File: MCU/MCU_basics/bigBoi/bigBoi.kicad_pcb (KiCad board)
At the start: 2 copper layers, 62 x 62 mm, 86 parts, among them IC1 BMP390, J3 DM3AT-SF-PEJM5_40_, J4 Conn_01x05, J5 Conn_01x04, J6 Conn_01x06, J7 USB_B_Micro, SW1 Boot Switch, U1 STM32F469NIHx, U2 LT1963AxST-3.3, U3 SX1276, U5 MIA-M10Q, U6 BNO086, Y1 8MHz, Y3 32kHz

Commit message: update nebula FP
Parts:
- removed C1, C10, C12, C15, C16, C19, C2, C20, C22, C23, C24, C25, C26, C3, C30, C35, C37, C39, C4, C48, C49, C5, C50, C51, C52, C54, C6, C7, C8, C9: 100nF, Capacitor_SMD:C_0402_1005Metric
- removed C11: 10nF, Capacitor_SMD:C_0402_1005Metric
- removed C13, C29, C31, C32, C38: 1uF, Capacitor_SMD:C_0402_1005Metric
- removed C14, C18: 0402, Capacitor_SMD:C_0402_1005Metric
- removed C17, C21: 2.2uF, Capacitor_SMD:C_0603_1608Metric
- removed C27, C59: 10uF, Capacitor_SMD:C_0805_2012Metric
- removed C28, C47: 15pF, Capacitor_SMD:C_0402_1005Metric
- removed C33, C34: 22uF, Capacitor_SMD:C_0805_2012Metric
- removed C36: 10uF, Capacitor_SMD:C_0603_1608Metric
- removed C40, C41, C43: 0.1uF, Capacitor_SMD:C_0402_1005Metric
- removed C42: 22pF, Capacitor_SMD:C_0402_1005Metric
- removed C44: 22PF, Capacitor_SMD:C_0402_1005Metric
- removed C45, C46: 100nf, Capacitor_SMD:C_0402_1005Metric
- removed C53, C58: 47pF, Capacitor_SMD:C_0402_1005Metric
- removed C55: 1.5pF, Capacitor_SMD:C_0402_1005Metric
- removed C56: 4.7pF, Capacitor_SMD:C_0402_1005Metric
- removed C57: 1nF, Capacitor_SMD:C_0402_1005Metric
- removed D1: 1N914, Diode_THT:D_DO-35_SOD27_P7.62mm_Horizontal
- removed D2: GREEN, LED_SMD:LED_0603_1608Metric
- removed FB1: 120R, Inductor_SMD:L_0603_1608Metric
- removed IC1: BMP390, Nebula-footprints:BMP390
- removed J3: DM3AT-SF-PEJM5_40_, Nebula-footprints:DM3ATSFPEJM540
- removed J4: Conn_01x05, Connector_PinHeader_2.54mm:PinHeader_1x05_P2.54mm_Vertical
- removed J5: Conn_01x04, Connector_PinHeader_2.54mm:PinHeader_1x04_P2.54mm_Vertical
- removed J6: Conn_01x06, Connector_PinHeader_2.54mm:PinHeader_1x06_P2.54mm_Vertical
- removed J7: USB_B_Micro, Connector_USB:USB_Micro-B_Molex_47346-0001
- removed R1, R2, R3, R4: 10k, Resistor_SMD:R_0402_1005Metric
- removed R5, R6: 2.2k, Resistor_SMD:R_0402_1005Metric
- removed R7: 1k5, Resistor_SMD:R_0402_1005Metric
- removed the REF** at (152.3, 118.0)
- removed the REF** at (105.5, 118.0)
- removed SW1: Boot Switch, Button_Switch_SMD:SW_SPDT_PCM12
- removed U1: STM32F469NIHx, Package_BGA:TFBGA-216_13x13mm_Layout15x15_P0.8mm
- removed U2: LT1963AxST-3.3, Package_TO_SOT_SMD:SOT-223-3_TabPin2
- removed U3: SX1276, Package_DFN_QFN:QFN-28-1EP_6x6mm_P0.65mm_EP4.8x4.8mm
- removed U5: MIA-M10Q, Package_LGA:ublox_LGA-53_4.5x4.5mm_Layout9x9_P0.5mm
- removed U6: BNO086, Nebula-footprints:BNO086
- removed Y1: 8MHz, Crystal:Crystal_SMD_3225-4Pin_3.2x2.5mm_HandSoldering
- removed Y3: 32kHz, Crystal:Crystal_SMD_3215-2Pin_3.2x1.5mm

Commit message: Bat
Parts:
- removed the REF** at (128.9, 77.5)
- added REF**: MountingHole_3.2mm_M3, MountingHole:MountingHole_3.2mm_M3, F.Cu at (140.0, 100.0)
- added REF**: MountingHole_3.2mm_M3, MountingHole:MountingHole_3.2mm_M3, F.Cu at (108.0, 132.0)
- added REF**: MountingHole_3.2mm_M3, MountingHole:MountingHole_3.2mm_M3, F.Cu at (108.0, 68.0)
- added REF**: MountingHole_3.2mm_M3, MountingHole:MountingHole_3.2mm_M3, F.Cu at (76.0, 100.0)
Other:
- board size 62 x 62 mm -> 70 x 70 mm

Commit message: small changes
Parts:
- added BT1: Battery, Connector_JST:JST_PH_S2B-PH-K_1x02_P2.00mm_Horizontal, F.Cu at (178.0, 93.5)
- added C1: 100nF, Capacitor_SMD:C_0402_1005Metric, F.Cu at (105.6, 76.5)
- added C10: 100nF, Capacitor_SMD:C_0402_1005Metric, F.Cu at (108.4, 78.5)
- added C11: 10nF, Capacitor_SMD:C_0402_1005Metric, F.Cu at (108.4, 80.4)
- added C12: 100nF, Capacitor_SMD:C_0402_1005Metric, F.Cu at (108.4, 82.4)
- added C13: 1uF, Capacitor_SMD:C_0402_1005Metric, F.Cu at (108.4, 84.4)
- added C14: 0402, Capacitor_SMD:C_0402_1005Metric, F.Cu at (108.4, 86.3)
- added C15: 100nF, Capacitor_SMD:C_0402_1005Metric, F.Cu at (108.4, 88.3)
- added C16: 100nF, Capacitor_SMD:C_0402_1005Metric, F.Cu at (108.4, 90.3)
- added C17: 2.2uF, Capacitor_SMD:C_0603_1608Metric, F.Cu at (109.7, 92.8)
- added C18: 0402, Capacitor_SMD:C_0402_1005Metric, F.Cu at (111.3, 76.5)
- added C19: 100nF, Capacitor_SMD:C_0402_1005Metric, F.Cu at (111.3, 78.5)
- added C2: 100nF, Capacitor_SMD:C_0402_1005Metric, F.Cu at (105.6, 78.5)
- added C20: 100nF, Capacitor_SMD:C_0402_1005Metric, F.Cu at (111.3, 80.4)
- added C21: 2.2uF, Capacitor_SMD:C_0603_1608Metric, F.Cu at (109.7, 95.3)
- added C22: 100nF, Capacitor_SMD:C_0402_1005Metric, F.Cu at (111.3, 82.4)
- added C23: 100nF, Capacitor_SMD:C_0402_1005Metric, F.Cu at (111.3, 84.4)
- added C24: 100nF, Capacitor_SMD:C_0402_1005Metric, F.Cu at (111.3, 86.3)
- added C25: 100nF, Capacitor_SMD:C_0402_1005Metric, F.Cu at (111.3, 88.3)
- added C26: 100nF, Capacitor_SMD:C_0402_1005Metric, F.Cu at (111.3, 90.3)
- added C27: 10uF, Capacitor_SMD:C_0805_2012Metric, F.Cu at (85.7, 94.3)
- added C28: 15pF, Capacitor_SMD:C_0402_1005Metric, F.Cu at (119.1, 76.5)
- added C29: 1uF, Capacitor_SMD:C_0402_1005Metric, F.Cu at (114.2, 76.5)
- added C3: 100nF, Capacitor_SMD:C_0402_1005Metric, F.Cu at (105.6, 80.4)
- added C30: 100nF, Capacitor_SMD:C_0402_1005Metric, F.Cu at (114.2, 78.5)
- added C31: 1uF, Capacitor_SMD:C_0402_1005Metric, F.Cu at (114.2, 80.4)
- added C32: 1uF, Capacitor_SMD:C_0402_1005Metric, F.Cu at (114.2, 82.4)
- added C33: 22uF, Capacitor_SMD:C_0805_2012Metric, F.Cu at (129.7, 90.3)
- added C34: 22uF, Capacitor_SMD:C_0805_2012Metric, F.Cu at (129.7, 93.3)
- added C35: 100nF, Capacitor_SMD:C_0402_1005Metric, F.Cu at (115.1, 115.3)
- added C36: 10uF, Capacitor_SMD:C_0603_1608Metric, F.Cu at (115.7, 113.1)
- added C37: 100nF, Capacitor_SMD:C_0402_1005Metric, F.Cu at (115.1, 117.3)
- added C38: 1uF, Capacitor_SMD:C_0402_1005Metric, F.Cu at (102.7, 109.3)
- added C39: 100nF, Capacitor_SMD:C_0402_1005Metric, F.Cu at (102.7, 111.3)
- added C4: 100nF, Capacitor_SMD:C_0402_1005Metric, F.Cu at (105.6, 82.4)
- added C40: 0.1uF, Capacitor_SMD:C_0402_1005Metric, F.Cu at (121.1, 109.3)
- added C41: 0.1uF, Capacitor_SMD:C_0402_1005Metric, F.Cu at (121.1, 111.3)
- added C42: 22pF, Capacitor_SMD:C_0402_1005Metric, F.Cu at (121.1, 113.2)
- added C43: 0.1uF, Capacitor_SMD:C_0402_1005Metric, F.Cu at (121.1, 115.2)
- added C44: 22PF, Capacitor_SMD:C_0402_1005Metric, F.Cu at (121.1, 117.2)
- added C45: 100nf, Capacitor_SMD:C_0402_1005Metric, F.Cu at (124.2, 102.1)
- added C46: 100nf, Capacitor_SMD:C_0402_1005Metric, F.Cu at (124.2, 104.1)
- added C47: 15pF, Capacitor_SMD:C_0402_1005Metric, F.Cu at (119.1, 78.5)
- added C48: 100nF, Capacitor_SMD:C_0402_1005Metric, F.Cu at (119.1, 80.4)
- added C49: 100nF, Capacitor_SMD:C_0402_1005Metric, F.Cu at (119.1, 82.4)
- added C5: 100nF, Capacitor_SMD:C_0402_1005Metric, F.Cu at (105.6, 84.4)
- added C50: 100nF, Capacitor_SMD:C_0402_1005Metric, F.Cu at (119.1, 84.4)
- added C51: 100nF, Capacitor_SMD:C_0402_1005Metric, F.Cu at (121.9, 76.5)
- added C52: 100nF, Capacitor_SMD:C_0402_1005Metric, F.Cu at (121.9, 78.5)
- added C53: 47pF, Capacitor_SMD:C_0402_1005Metric, F.Cu at (121.9, 80.4)
- added C54: 100nF, Capacitor_SMD:C_0402_1005Metric, F.Cu at (121.9, 82.4)
- added C55: 1.5pF, Capacitor_SMD:C_0402_1005Metric, F.Cu at (121.9, 84.4)
- added C56: 4.7pF, Capacitor_SMD:C_0402_1005Metric, F.Cu at (124.8, 76.5)
- added C57: 1nF, Capacitor_SMD:C_0402_1005Metric, F.Cu at (124.8, 78.5)
- added C58: 47pF, Capacitor_SMD:C_0402_1005Metric, F.Cu at (124.8, 80.4)
- added C59: 10uF, Capacitor_SMD:C_0805_2012Metric, F.Cu at (128.5, 85.3)
- added C6: 100nF, Capacitor_SMD:C_0402_1005Metric, F.Cu at (105.6, 86.3)
- added C7: 100nF, Capacitor_SMD:C_0402_1005Metric, F.Cu at (105.6, 88.3)
- added C8: 100nF, Capacitor_SMD:C_0402_1005Metric, F.Cu at (105.6, 90.3)
- added C9: 100nF, Capacitor_SMD:C_0402_1005Metric, F.Cu at (108.4, 76.5)
- added D1: 1N914, Diode_THT:D_DO-35_SOD27_P7.62mm_Horizontal, F.Cu at (107.7, 110.1)
- added D2: GREEN, LED_SMD:LED_0603_1608Metric, F.Cu at (129.5, 96.1)
- added FB1: 120R, Inductor_SMD:L_0603_1608Metric, F.Cu at (109.7, 97.8)
- added IC1: BMP390, Nebula-footprints:BMP390, F.Cu at (120.2, 103.7)
- added J1: Conn_Coaxial, Connector_Coaxial:U.FL_Hirose_U.FL-R-SMT-1_Vertical, F.Cu at (183.3, 79.9)
- added J2: Conn_Coaxial, Connector_Coaxial:U.FL_Hirose_U.FL-R-SMT-1_Vertical, F.Cu at (164.8, 79.9)
- added J3: DM3AT-SF-PEJM5_40_, Nebula-footprints:DM3ATSFPEJM540, F.Cu at (95.2, 112.1)
- added J4: Conn_01x05, Connector_PinHeader_2.54mm:PinHeader_1x05_P2.54mm_Vertical, F.Cu at (90.4, 93.8)
- added J5: Conn_01x04, Connector_PinHeader_2.54mm:PinHeader_1x04_P2.54mm_Vertical, F.Cu at (95.0, 93.8)
- added J6: Conn_01x06, Connector_PinHeader_2.54mm:PinHeader_1x06_P2.54mm_Vertical, F.Cu at (85.8, 77.8)
- added J7: USB_B_Micro, Connector_USB:USB_Micro-B_Molex_47346-0001, F.Cu at (102.5, 94.7)
- added R1: 10k, Resistor_SMD:R_0402_1005Metric, F.Cu at (85.0, 96.8)
- added R2: 10k, Resistor_SMD:R_0402_1005Metric, F.Cu at (132.1, 84.8)
- added R3: 10k, Resistor_SMD:R_0402_1005Metric, F.Cu at (115.1, 119.3)
- added R4: 10k, Resistor_SMD:R_0402_1005Metric, F.Cu at (130.9, 109.3)
- added R5: 2.2k, Resistor_SMD:R_0402_1005Metric, F.Cu at (130.9, 111.3)
- added R6: 2.2k, Resistor_SMD:R_0402_1005Metric, F.Cu at (130.9, 113.3)
- added R7: 1k5, Resistor_SMD:R_0402_1005Metric, F.Cu at (119.1, 98.1)
- added SW1: Boot Switch, Button_Switch_SMD:SW_SPDT_PCM12, F.Cu at (102.2, 102.1)
- added U1: STM32F469NIHx, Package_BGA:TFBGA-216_13x13mm_Layout15x15_P0.8mm, F.Cu at (96.1, 83.5)
- added U2: LT1963AxST-3.3, Package_TO_SOT_SMD:SOT-223-3_TabPin2, F.Cu at (122.5, 93.0)
- added U3: SX1276, Package_DFN_QFN:QFN-28-1EP_6x6mm_P0.65mm_EP4.8x4.8mm, F.Cu at (130.8, 79.7)
- added U5: MIA-M10Q, Nebula-footprints:MIA-M10Q, F.Cu at (109.9, 115.6)
- added U6: BNO086, Nebula-footprints:BNO086, F.Cu at (126.0, 112.5)
- added Y1: 8MHz, Crystal:Crystal_SMD_3225-4Pin_3.2x2.5mm_HandSoldering, F.Cu at (111.0, 102.0)
- added Y3: 32kHz, Crystal:Crystal_SMD_3215-2Pin_3.2x1.5mm, F.Cu at (125.1, 118.3)

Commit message: Via escape routing
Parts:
- added GPS_BT1: CR1220, Battery:BatteryHolder_Keystone_500, F.Cu at (155.1, 57.1)
- added L1: 10nH, Inductor_SMD:L_0402_1005Metric, F.Cu at (154.0, 68.6)
- added L2: 10nH, Inductor_SMD:L_0402_1005Metric, F.Cu at (154.0, 70.6)
- added L3: 6.2nH, Inductor_SMD:L_0402_1005Metric, F.Cu at (154.0, 72.6)
- added U4: PE4259, Nebula-footprints:SOT65P215X110-6N, F.Cu at (157.7, 74.0)
- added Y2: 32MHz, Crystal:Crystal_SMD_3225-4Pin_3.2x2.5mm, F.Cu at (158.0, 69.9)
- C1, C2, C3, C4, C5, C8: moved to B.Cu
- C14, C18: value 0402 -> 15pF
- U3: footprint Package_DFN_QFN:QFN-28-1EP_6x6mm_P0.65mm_EP4.8x4.8mm -> Nebula-footprints:QFN65P600X600X100-29N
- moved C28 68.8 mm to (61.2, 39.2)
- moved C47 68.8 mm to (61.2, 41.1)
- moved C48 68.8 mm to (61.2, 43.1)
- moved C56 68.8 mm to (67.0, 39.2)
- moved C57 68.8 mm to (67.0, 41.1)
- moved C58 68.8 mm to (67.0, 43.1)
- moved C59 68.8 mm to (70.6, 48.0)
- moved J4 68.8 mm to (32.5, 56.5)
- moved R4 68.8 mm to (73.1, 72.0)
- moved R6 68.8 mm to (73.1, 76.0)
- moved Y1 68.8 mm to (53.2, 64.6)
- moved Y3 68.8 mm to (67.2, 81.0)
- moved C16 68.8 mm to (50.6, 53.0)
- moved C17 68.8 mm to (51.9, 55.5)
- moved C26 68.8 mm to (53.5, 53.0)
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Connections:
- J3 pad 6: <NO NET> -> GND
- J3 pad MP1: <NO NET> -> GND
- J3 pad MP2: <NO NET> -> GND
- J3 pad MP3: <NO NET> -> GND
- J3 pad MP4: <NO NET> -> GND
- J3 pad MP5: <NO NET> -> GND
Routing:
- net +3.3V: track 0.00 -> 0.24 mm, vias 0 -> 20
- net BNO086_WAKE/PS0_N: track 0.00 -> 0.10 mm, vias 0 -> 1
- net BMP390_CS_N: track 0.00 -> 0.10 mm, vias 0 -> 1
- net GND: track 0.00 -> 0.10 mm, vias 0 -> 22
- net SX1276_SCK_N: vias 0 -> 1
- net SX1276_MISO_N: vias 0 -> 1
- net Net-(U1-VCAP2): vias 0 -> 1
- net Net-(U1-VCAP1): vias 0 -> 1
- net Net-(U1-PDR_ON): vias 0 -> 1
- net Net-(U1-BOOT0): vias 0 -> 1
- net GPS_TX_N: vias 0 -> 1
- net GPS_RX_N: vias 0 -> 1
- net DM3AT_MOSI_0: vias 0 -> 1
- net BNO086_NRST_N: vias 0 -> 1
- net BNO086_INTN_N: vias 0 -> 1
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- added copper zone on In2.Cu, net +3.3V
- added copper zone on In1.Cu, net GND
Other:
- copper layers 2 -> 4

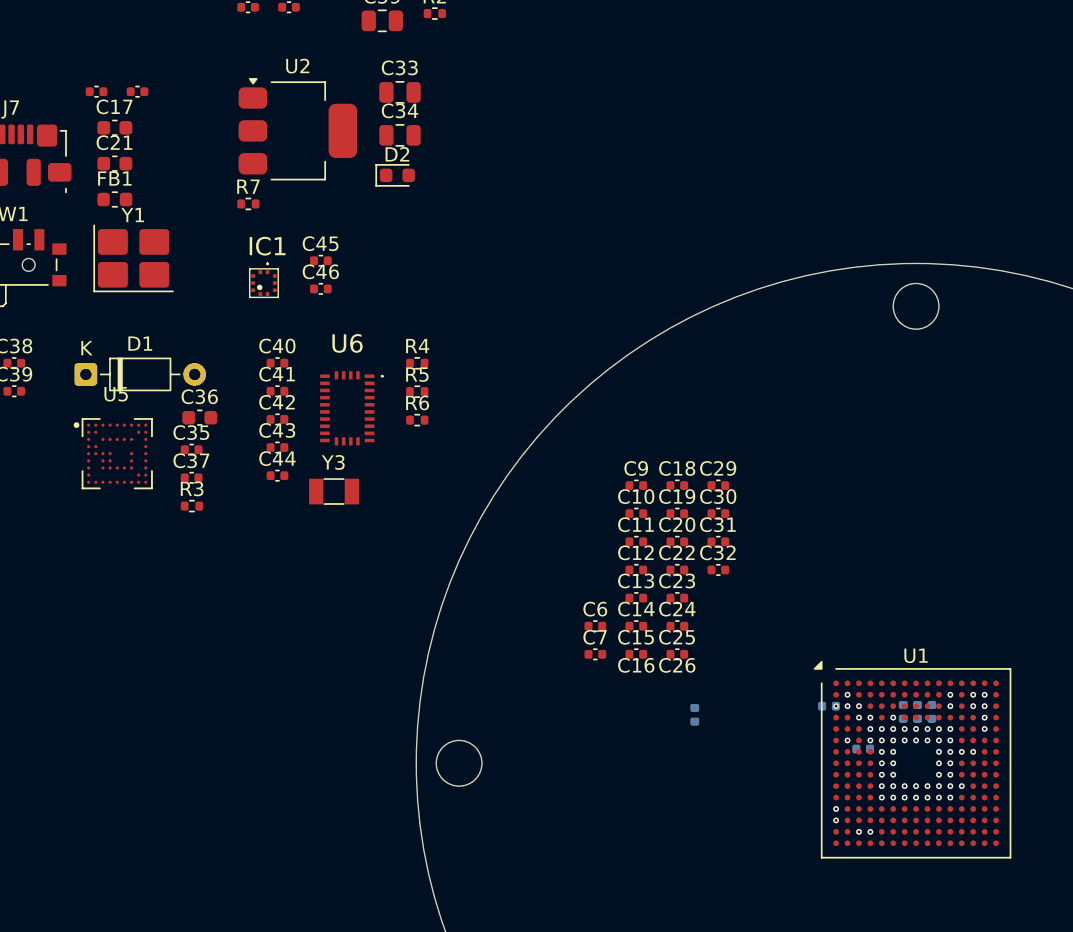
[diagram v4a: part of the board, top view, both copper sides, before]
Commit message: decoupling cap placement
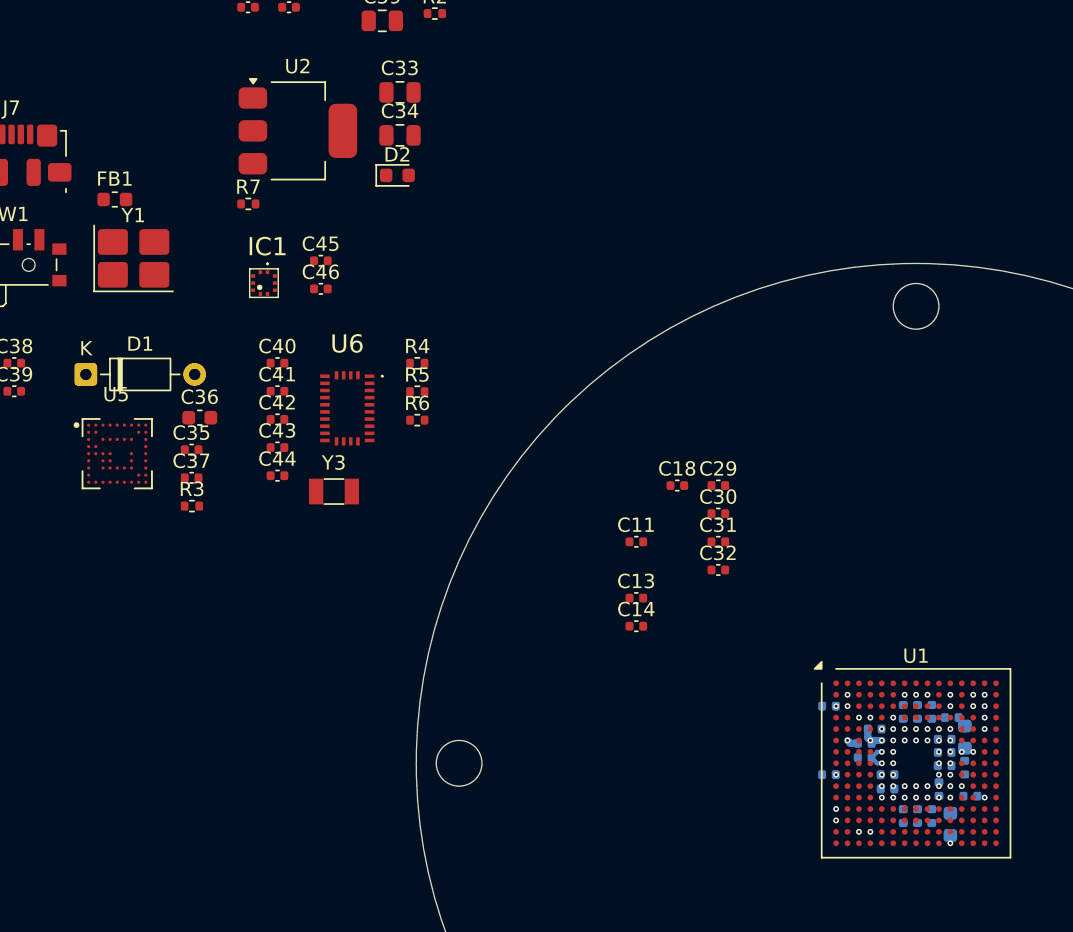
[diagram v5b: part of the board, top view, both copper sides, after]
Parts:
- C10, C12, C15, C16, C17, C19, C20, C21, C22, C23, C24, C25, C26, C6, C7, C9: moved to B.Cu
- moved C16 77.4 mm to (109.1, 103.7), turned to -90 degrees
- moved C17 76.2 mm to (110.4, 104.3), turned to -90 degrees
- moved C21 71.8 mm to (111.4, 98.2), turned to 90 degrees
- moved C26 68.4 mm to (104.4, 98.6), turned to 180 degrees
- moved C9 29.2 mm to (110.0, 100.2), turned to 180 degrees
- moved C10 29.1 mm to (111.4, 100.3), turned to 90 degrees
- moved C12 28.2 mm to (111.8, 102.3)
- moved C6 25.8 mm to (110.5, 96.8)
- moved C20 25.5 mm to (108.1, 103.7), turned to -90 degrees
- moved C7 25.2 mm to (110.0, 98.3), turned to 180 degrees
- moved C15 23.2 mm to (109.6, 101.8), turned to 90 degrees
- moved C23 22.0 mm to (107.1, 103.7), turned to -90 degrees
- moved C19 20.5 mm to (105.1, 97.6)
- moved C24 18.6 mm to (106.0, 101.8)
- moved C22 17.8 mm to (101.9, 100.8)
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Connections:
- U1 pad A4: unconnected-(U1-PG14-PadA4) -> BNO086_INTN_N
- U1 pad B7: unconnected-(U1-PG15-PadB7) -> GND
- U1 pad B8: unconnected-(U1-PG11-PadB8) -> GND
- U1 pad B9: unconnected-(U1-PJ13-PadB9) -> GND
- U1 pad C3: BNO086_INTN_N -> unconnected-(U1-PI4-PadC3)
- U1 pad E4: BNO086_WAKE/PS0_N -> unconnected-(U1-PI9-PadE4)
- U1 pad F1: unconnected-(U1-PC15-PadF1) -> BNO086_WAKE/PS0_N
- U1 pad L14: unconnected-(U1-PD9-PadL14) -> GND
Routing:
- net +3.3V: track 0.24 -> 3.81 mm, vias 20 -> 21
- net GND: track 0.10 -> 0.90 mm, vias 22 -> 26
- net BNO086_WAKE/PS0_N: track 0.10 -> 0.00 mm, vias 1 -> 0
- net Net-(U1-NRST): vias 0 -> 1
- net BNO086_INTN_N: vias 1 -> 0

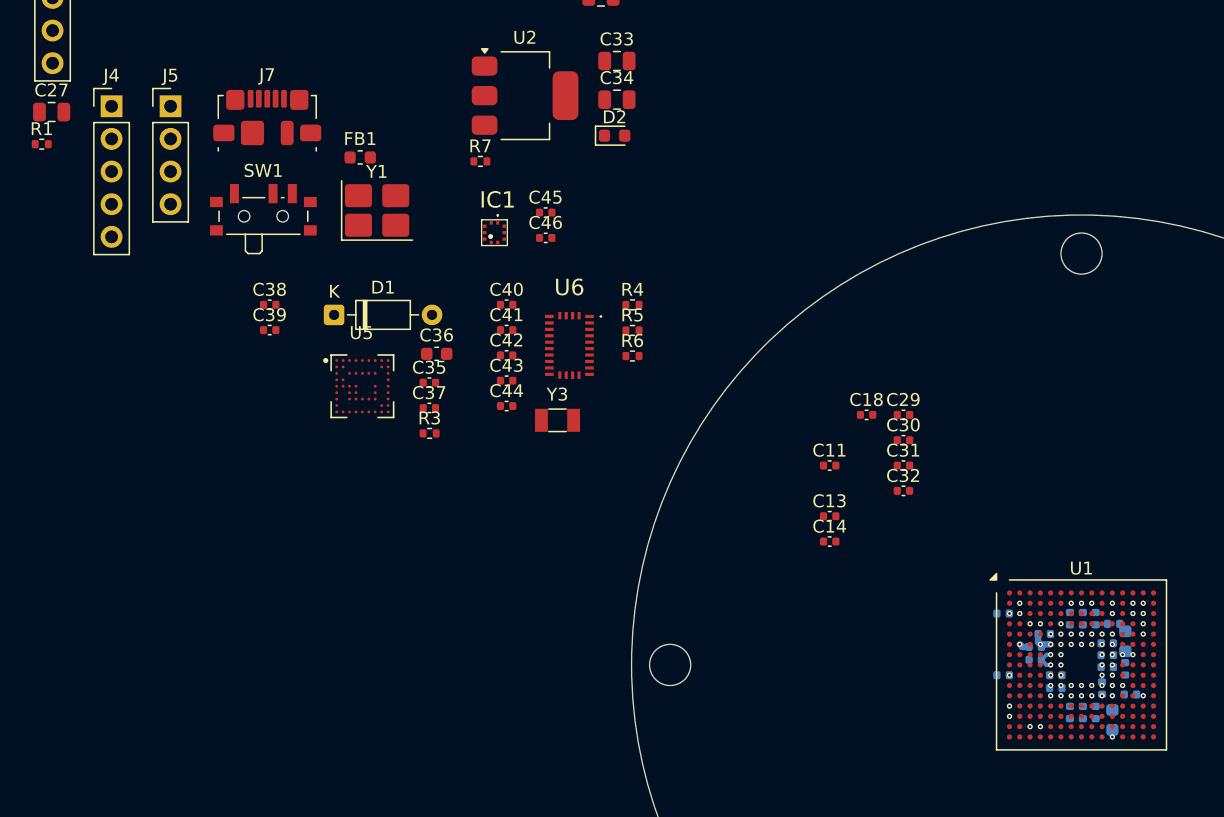
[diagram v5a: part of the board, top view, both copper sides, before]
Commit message: MCU pwr+esc
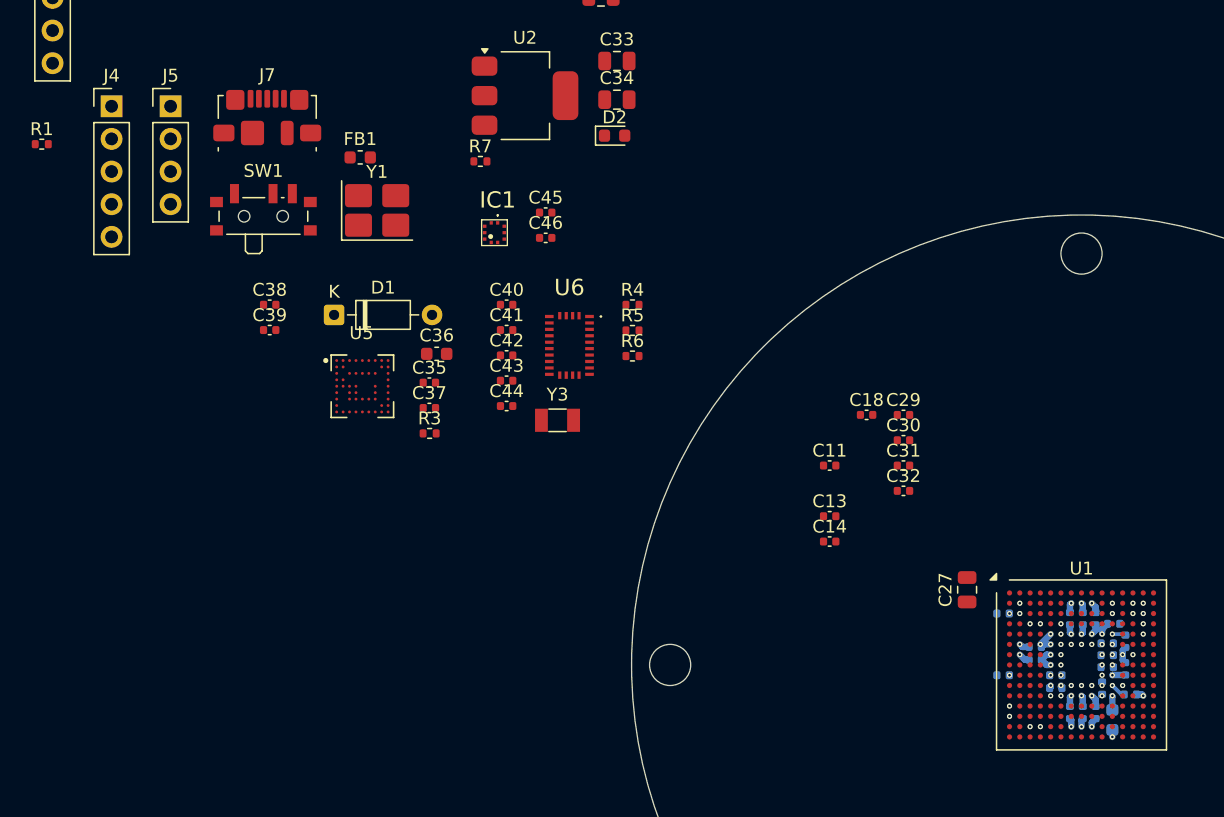
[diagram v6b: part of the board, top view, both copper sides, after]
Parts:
- removed C19: 100nF, Capacitor_SMD:C_0402_1005Metric
- C21: value 2.2uF -> 1uF; footprint Capacitor_SMD:C_0603_1608Metric -> Capacitor_SMD:C_0402_1005Metric
- moved C27 80.3 mm to (99.1, 94.2), turned to 90 degrees
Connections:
- U1 pad E5: Net-(U1-PDR_ON) -> +3.3V
- U1 pad G2: unconnected-(U1-PF2-PadG2) -> GND
- U1 pad P7: unconnected-(U1-PJ2-PadP7) -> GND
- U1 pad P8: unconnected-(U1-PF11-PadP8) -> GND
- U1 pad P9: unconnected-(U1-PE9-PadP9) -> GND
- U1 pad R11: unconnected-(U1-PE15-PadR11) -> GND
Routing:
- net +3.3V: track 3.81 -> 12.5 mm
- net GND: track 0.90 -> 8.89 mm, vias 26 -> 31
- net Net-(U1-VCAP1): track 0.00 -> 1.09 mm
- net Net-(U1-VCAP2): track 0.12 -> 1.05 mm
- net Net-(U1-PDR_ON): vias 1 -> 0

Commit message: Store deler av VBUS og USB
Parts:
- added C19: 100nF, Capacitor_SMD:C_0402_1005Metric, F.Cu at (128.8, 102.2)
- added U7: USBLC6-2SC6, Package_TO_SOT_SMD:SOT-23-6, F.Cu at (126.7, 99.1)
- moved J7 97.6 mm to (132.5, 100.0), turned to 90 degrees
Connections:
- J7 pad 2: Net-(J7-D-) -> /D-
- J7 pad 3: Net-(J7-D+) -> /D+
- J7 pad 4: unconnected-(J7-ID-Pad4) -> GND
- U1 pad B15: Net-(J7-D+) -> /DMCU+
- U1 pad C15: Net-(J7-D-) -> /DMCU-
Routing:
- net /DMCU+: track 0.00 -> 13.8 mm
- net /DMCU-: track 0.00 -> 13.6 mm
- net VBUS: track 0.00 -> 8.04 mm
- net GND: track 8.89 -> 14.1 mm, vias 31 -> 35
- net /D+: track 0.00 -> 4.26 mm
- net /D-: track 0.00 -> 3.64 mm
- net +3.3V: track 12.5 -> 13.5 mm, vias 21 -> 22
